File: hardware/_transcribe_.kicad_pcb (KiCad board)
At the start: 2 copper layers, 100 x 45 mm, 27 parts, among them J1 europower, J2 stereo_jack_3.5mm, J3 dsub9_socket, J4 stereo_jack_3.5mm, J5 din5, J6 stereo_jack_3.5mm, J7 din5, J8 Conn_01x06, J9 Conn_02x03_Odd_Even, SW1 SW_Push_Dual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

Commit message: update bom
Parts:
- added J10: jumper, Connector_PinHeader_2.54mm:PinHeader_1x03_P2.54mm_Vertical, F.Cu at (-254.9, -749.4)
- J8: value Conn_01x06 -> bootloader
- J9: value Conn_02x03_Odd_Even -> jumper; footprint Connector_PinHeader_2.54mm:PinHeader_2x03_P2.54mm_Vertical -> Connector_PinHeader_2.54mm:PinHeader_1x03_P2.54mm_Vertical
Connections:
- J3 pad 2: Net-(J3-Pad2) -> Net-(J10-Pad1)
- J3 pad 3: Net-(J3-Pad3) -> Net-(J10-Pad3)
- J9 pad 1: Net-(J3-Pad3) -> Net-(J10-Pad3)
- J9 pad 2: Net-(J3-Pad2) -> RS_SERIAL_OUT
- J9 pad 3: RS_SERIAL_OUT -> Net-(J10-Pad1)
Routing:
- net Net-(J3-Pad3): track 33.3 -> 0.00 mm
- net Net-(J10-Pad3): track 0.00 -> 33.3 mm
- net Net-(J3-Pad2): track 26.2 -> 0.00 mm
- net Net-(J10-Pad1): track 0.00 -> 26.2 mm

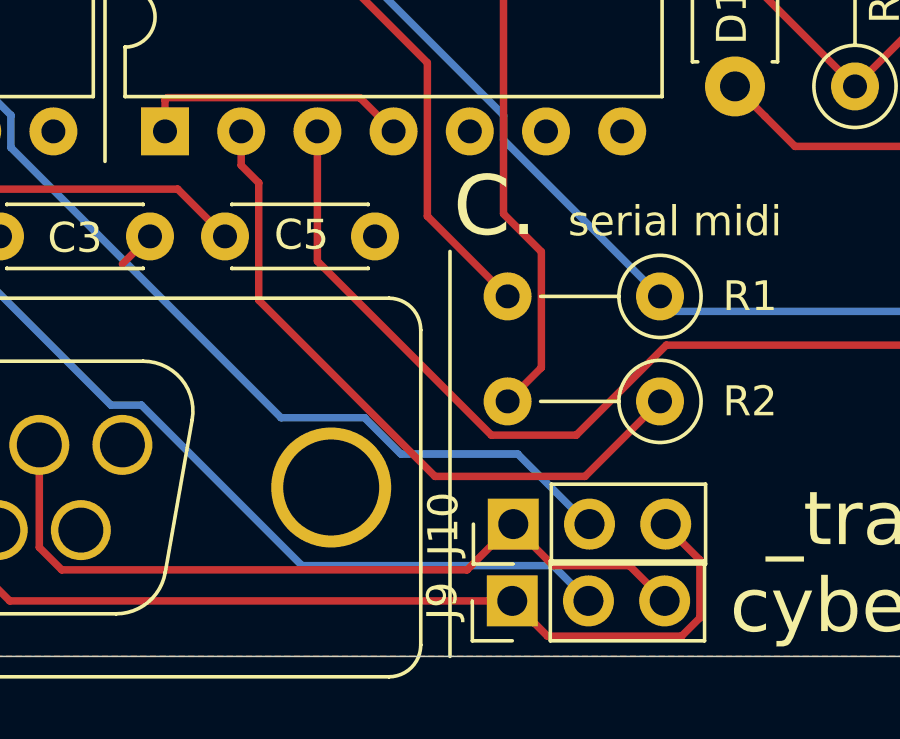
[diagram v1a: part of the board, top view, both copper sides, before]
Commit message: add booklet
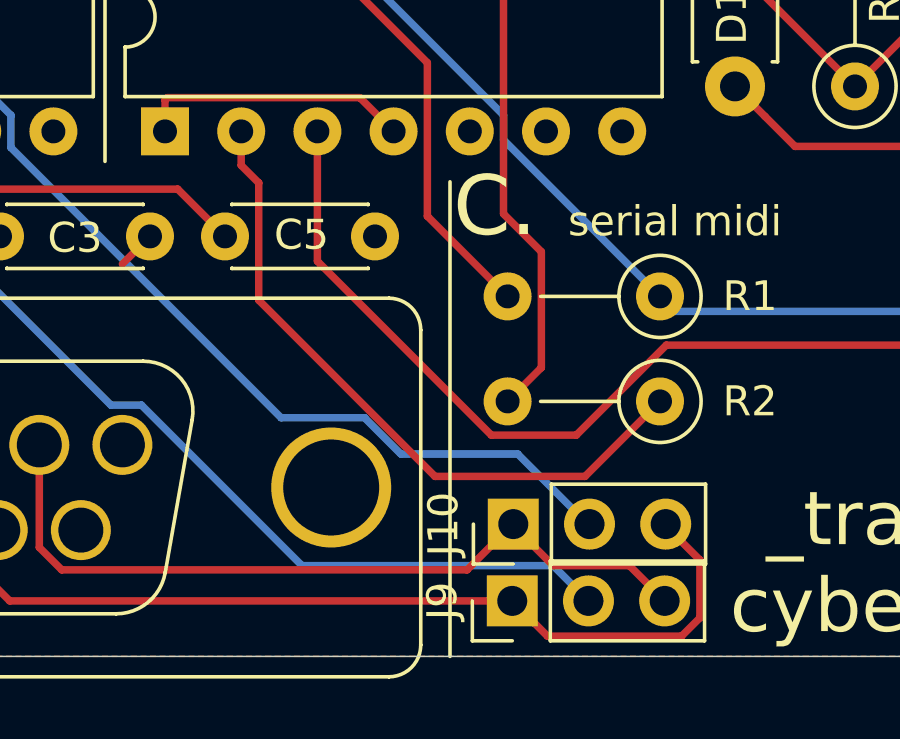
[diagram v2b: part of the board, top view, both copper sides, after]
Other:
- board text added: "JLCJLCJLCJLC"

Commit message: uncomment the code
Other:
- net class Default removed
